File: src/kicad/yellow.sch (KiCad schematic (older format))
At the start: 3 parts, among them U10 74HC08, U8 74HC08, U9 74HC08

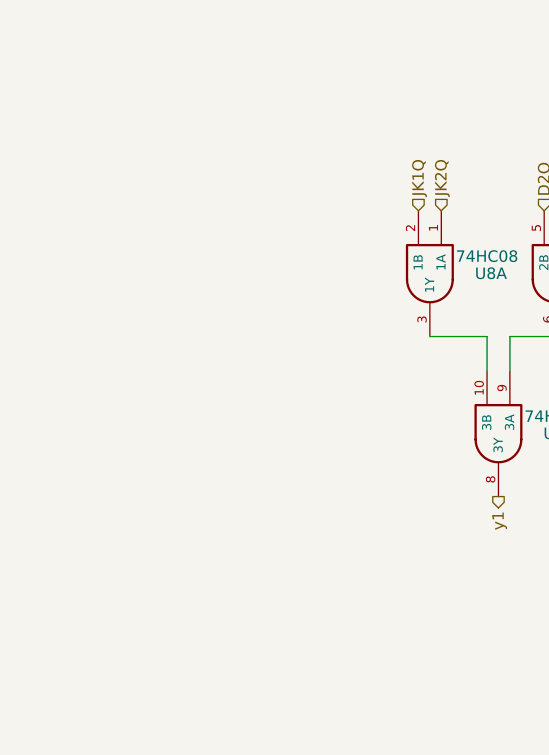
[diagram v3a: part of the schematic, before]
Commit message: added annotations, power connections to parts
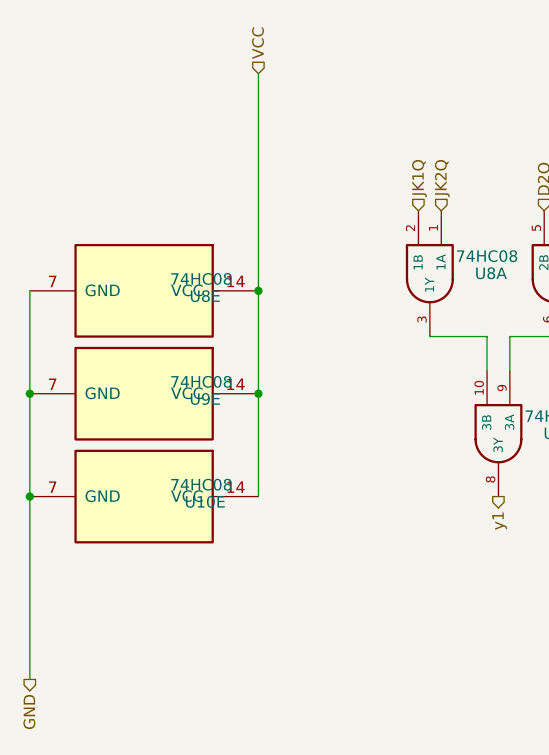
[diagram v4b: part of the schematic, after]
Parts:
- added unit 5 of U10
- added unit 5 of U8
- added unit 5 of U9
- U10, U8, U9: footprint Housings_SOIC:SOIC-14_3.9x8.7mm_Pitch1.27mm -> Package_SO:SOIC-14_3.9x8.7mm_P1.27mm
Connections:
- new net GND: U10.7 (GND), U8.7 (GND), U9.7 (GND)
- new net VCC: U10.14 (VCC), U8.14 (VCC), U9.14 (VCC)
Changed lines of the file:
@@
 F 0 "U8" V 2475 3117 50  0000 C CNN
 F 1 "74HC08" V 2400 3100 50  0000 C CNN
-F 2 "Housings_SOIC:SOIC-14_3.9x8.7mm_Pitch1.27mm" H 2450 2850 50  0001 C CNN
+F 2 "Package_SO:SOIC-14_3.9x8.7mm_P1.27mm" H 2450 2850 50  0001 C CNN
 F 3 "https://datasheet.lcsc.com/szlcsc/Nexperia-74HC08D-653_C5593.pdf" H 2450 2850 50  0001 C CNN
 F 4 "C5593" H 2450 2850 50  0001 C CNN "LCSC"
@@
 F 0 "U8" V 3025 3117 50  0000 C CNN
 F 1 "74HC08" V 2950 3100 50  0000 C CNN
-F 2 "Housings_SOIC:SOIC-14_3.9x8.7mm_Pitch1.27mm" H 3000 2850 50  0001 C CNN
+F 2 "Package_SO:SOIC-14_3.9x8.7mm_P1.27mm" H 3000 2850 50  0001 C CNN
 F 3 "https://datasheet.lcsc.com/szlcsc/Nexperia-74HC08D-653_C5593.pdf" H 3000 2850 50  0001 C CNN
 F 4 "C5593" H 3000 2850 50  0001 C CNN "LCSC"
@@
 F 0 "U8" V 2775 3817 50  0000 C CNN
 F 1 "74HC08" V 2700 3800 50  0000 C CNN
-F 2 "Housings_SOIC:SOIC-14_3.9x8.7mm_Pitch1.27mm" H 2750 3550 50  0001 C CNN
+F 2 "Package_SO:SOIC-14_3.9x8.7mm_P1.27mm" H 2750 3550 50  0001 C CNN
 F 3 "https://datasheet.lcsc.com/szlcsc/Nexperia-74HC08D-653_C5593.pdf" H 2750 3550 50  0001 C CNN
 F 4 "C5593" H 2750 3550 50  0001 C CNN "LCSC"
@@
 F 0 "U8" V 3825 3167 50  0000 C CNN
 F 1 "74HC08" V 3750 3150 50  0000 C CNN
-F 2 "Housings_SOIC:SOIC-14_3.9x8.7mm_Pitch1.27mm" H 3800 2900 50  0001 C CNN
+F 2 "Package_SO:SOIC-14_3.9x8.7mm_P1.27mm" H 3800 2900 50  0001 C CNN
 F 3 "https://datasheet.lcsc.com/szlcsc/Nexperia-74HC08D-653_C5593.pdf" H 3800 2900 50  0001 C CNN
 F 4 "C5593" H 3800 2900 50  0001 C CNN "LCSC"
@@
 F 0 "U9" V 4475 3217 50  0000 C CNN
 F 1 "74HC08" V 4400 3200 50  0000 C CNN
-F 2 "Housings_SOIC:SOIC-14_3.9x8.7mm_Pitch1.27mm" H 4450 2950 50  0001 C CNN
+F 2 "Package_SO:SOIC-14_3.9x8.7mm_P1.27mm" H 4450 2950 50  0001 C CNN
 F 3 "https://datasheet.lcsc.com/szlcsc/Nexperia-74HC08D-653_C5593.pdf" H 4450 2950 50  0001 C CNN
 F 4 "C5593" H 4450 2950 50  0001 C CNN "LCSC"
@@
 F 0 "U9" V 4075 3817 50  0000 C CNN
 F 1 "74HC08" V 4000 3800 50  0000 C CNN
-F 2 "Housings_SOIC:SOIC-14_3.9x8.7mm_Pitch1.27mm" H 4050 3550 50  0001 C CNN
+F 2 "Package_SO:SOIC-14_3.9x8.7mm_P1.27mm" H 4050 3550 50  0001 C CNN
 F 3 "https://datasheet.lcsc.com/szlcsc/Nexperia-74HC08D-653_C5593.pdf" H 4050 3550 50  0001 C CNN
 F 4 "C5593" H 4050 3550 50  0001 C CNN "LCSC"
@@
 F 0 "U9" V 5275 3167 50  0000 C CNN
 F 1 "74HC08" V 5200 3150 50  0000 C CNN
-F 2 "Housings_SOIC:SOIC-14_3.9x8.7mm_Pitch1.27mm" H 5250 2900 50  0001 C CNN
+F 2 "Package_SO:SOIC-14_3.9x8.7mm_P1.27mm" H 5250 2900 50  0001 C CNN
 F 3 "https://datasheet.lcsc.com/szlcsc/Nexperia-74HC08D-653_C5593.pdf" H 5250 2900 50  0001 C CNN
 F 4 "C5593" H 5250 2900 50  0001 C CNN "LCSC"
@@
 F 0 "U9" V 5875 3217 50  0000 C CNN
 F 1 "74HC08" V 5800 3200 50  0000 C CNN
-F 2 "Housings_SOIC:SOIC-14_3.9x8.7mm_Pitch1.27mm" H 5850 2950 50  0001 C CNN
+F 2 "Package_SO:SOIC-14_3.9x8.7mm_P1.27mm" H 5850 2950 50  0001 C CNN
 F 3 "https://datasheet.lcsc.com/szlcsc/Nexperia-74HC08D-653_C5593.pdf" H 5850 2950 50  0001 C CNN
 F 4 "C5593" H 5850 2950 50  0001 C CNN "LCSC"
@@
 F 0 "U10" V 5575 3917 50  0000 C CNN
 F 1 "74HC08" V 5500 3900 50  0000 C CNN
-F 2 "Housings_SOIC:SOIC-14_3.9x8.7mm_Pitch1.27mm" H 5550 3650 50  0001 C CNN
+F 2 "Package_SO:SOIC-14_3.9x8.7mm_P1.27mm" H 5550 3650 50  0001 C CNN
 F 3 "https://datasheet.lcsc.com/szlcsc/Nexperia-74HC08D-653_C5593.pdf" H 5550 3650 50  0001 C CNN
 F 4 "C5593" H 5550 3650 50  0001 C CNN "LCSC"
@@
 F 0 "U10" V 6450 3200 50  0000 C CNN
 F 1 "74HC08" V 6350 3200 50  0000 C CNN
-F 2 "Housings_SOIC:SOIC-14_3.9x8.7mm_Pitch1.27mm" H 6400 2950 50  0001 C CNN
+F 2 "Package_SO:SOIC-14_3.9x8.7mm_P1.27mm" H 6400 2950 50  0001 C CNN
 F 3 "https://datasheet.lcsc.com/szlcsc/Nexperia-74HC08D-653_C5593.pdf" H 6400 2950 50  0001 C CNN
 F 4 "C5593" H 6400 2950 50  0001 C CNN "LCSC"
@@
 F 0 "U10" V 6975 3217 50  0000 C CNN
 F 1 "74HC08" V 6900 3200 50  0000 C CNN
-F 2 "Housings_SOIC:SOIC-14_3.9x8.7mm_Pitch1.27mm" H 6950 2950 50  0001 C CNN
+F 2 "Package_SO:SOIC-14_3.9x8.7mm_P1.27mm" H 6950 2950 50  0001 C CNN
 F 3 "https://datasheet.lcsc.com/szlcsc/Nexperia-74HC08D-653_C5593.pdf" H 6950 2950 50  0001 C CNN
 F 4 "C5593" H 6950 2950 50  0001 C CNN "LCSC"
@@
 F 0 "U10" V 6675 3967 50  0000 C CNN
 F 1 "74HC08" V 6600 3950 50  0000 C CNN
-F 2 "Housings_SOIC:SOIC-14_3.9x8.7mm_Pitch1.27mm" H 6650 3700 50  0001 C CNN
+F 2 "Package_SO:SOIC-14_3.9x8.7mm_P1.27mm" H 6650 3700 50  0001 C CNN
 F 3 "https://datasheet.lcsc.com/szlcsc/Nexperia-74HC08D-653_C5593.pdf" H 6650 3700 50  0001 C CNN
 F 4 "C5593" H 6650 3700 50  0001 C CNN "LCSC"
@@
 Text HLabel 7000 2700 1    50   Input ~ 0
 D2!Q
+$Comp
+L PB170:74HC08 U?
+U 5 1 6060BB07
+P 1200 2950
+AR Path="/6060BB07" Ref="U?"  Part="2"
+AR Path="/6006FC3B/6060BB07" Ref="U?"  Part="4"
+AR Path="/6004480C/6060BB07" Ref="U?"  Part="4"
+AR Path="/60019DBB/6060BB07" Ref="U8"  Part="5"
+F 0 "U8" V 1225 3217 50  0000 C CNN
+F 1 "74HC08" V 1150 3200 50  0000 C CNN
+F 2 "Package_SO:SOIC-14_3.9x8.7mm_P1.27mm" H 1200 2950 50  0001 C CNN
+F 3 "https://datasheet.lcsc.com/szlcsc/Nexperia-74HC08D-653_C5593.pdf" H 1200 2950 50  0001 C CNN
+F 4 "C5593" H 1200 2950 50  0001 C CNN "LCSC"
+	5    1200 2950
+	0    1    1    0
+$EndComp
+$Comp
+L PB170:74HC08 U?
+U 5 1 6060D9E8
+P 1200 3400
+AR Path="/6060D9E8" Ref="U?"  Part="2"
+AR Path="/6006FC3B/6060D9E8" Ref="U?"  Part="4"
+AR Path="/6004480C/6060D9E8" Ref="U?"  Part="4"
+AR Path="/60019DBB/6060D9E8" Ref="U9"  Part="5"
+F 0 "U9" V 1225 3667 50  0000 C CNN
+F 1 "74HC08" V 1150 3650 50  0000 C CNN
+F 2 "Package_SO:SOIC-14_3.9x8.7mm_P1.27mm" H 1200 3400 50  0001 C CNN
+F 3 "https://datasheet.lcsc.com/szlcsc/Nexperia-74HC08D-653_C5593.pdf" H 1200 3400 50  0001 C CNN
+F 4 "C5593" H 1200 3400 50  0001 C CNN "LCSC"
+	5    1200 3400
+	0    1    1    0
+$EndComp
+$Comp
+L PB170:74HC08 U?
+U 5 1 6060E9B8
+P 1200 3850
+AR Path="/6060E9B8" Ref="U?"  Part="2"
+AR Path="/6006FC3B/6060E9B8" Ref="U?"  Part="4"
+AR Path="/6004480C/6060E9B8" Ref="U?"  Part="4"
+AR Path="/60019DBB/6060E9B8" Ref="U10"  Part="5"
+F 0 "U10" V 1225 4117 50  0000 C CNN
+F 1 "74HC08" V 1150 4100 50  0000 C CNN
+F 2 "Package_SO:SOIC-14_3.9x8.7mm_P1.27mm" H 1200 3850 50  0001 C CNN
+F 3 "https://datasheet.lcsc.com/szlcsc/Nexperia-74HC08D-653_C5593.pdf" H 1200 3850 50  0001 C CNN
+F 4 "C5593" H 1200 3850 50  0001 C CNN "LCSC"
+	5    1200 3850
+	0    1    1    0
+$EndComp
+Wire Wire Line
+	700  3400 700  3850
+Connection ~ 700  3850
+Wire Wire Line
+	700  3850 700  4650
+Wire Wire Line
+	700  3400 700  2950
+Connection ~ 700  3400
+Wire Wire Line
+	1700 3850 1700 3400
+Wire Wire Line
+	1700 3400 1700 2950
+Connection ~ 1700 3400
+Wire Wire Line
+	1700 2950 1700 2000
+Connection ~ 1700 2950
+Text HLabel 1700 2000 1    50   Input ~ 0
+VCC
+Text HLabel 700  4650 3    50   Output ~ 0
+GND
 $EndSCHEMATC

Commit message: Corrected negations
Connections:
- net D2!Q renamed D2~Q
- net JK1!Q renamed JK1~Q
- net JK2!Q renamed JK2~Q
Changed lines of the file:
@@
 D2Q
 Text HLabel 4400 2700 1    50   Input ~ 0
-D2!Q
+D2~Q
 Text HLabel 2400 2600 1    50   Input ~ 0
 JK1Q
 Text HLabel 3750 2650 1    50   Input ~ 0
-JK1!Q
+JK1~Q
 Text HLabel 2500 2600 1    50   Input ~ 0
 JK2Q
 Text HLabel 5900 2700 1    50   Input ~ 0
-JK2!Q
+JK2~Q
 Text HLabel 2750 3850 3    50   Output ~ 0
 y1
@@
 JK2Q
 Text HLabel 4500 2700 1    50   Input ~ 0
-D2!Q
+D2~Q
 Text HLabel 5200 2650 1    50   Input ~ 0
-JK1!Q
+JK1~Q
 Text HLabel 5300 2650 1    50   Input ~ 0
 D2Q
 Text HLabel 6350 2700 1    50   Input ~ 0
-JK2!Q
+JK2~Q
 Text HLabel 6450 2700 1    50   Input ~ 0
 JK1Q
@@
 D1Q
 Text HLabel 7000 2700 1    50   Input ~ 0
-D2!Q
-$Comp
-L PB170:74HC08 U?
+D2~Q
+$Comp
+L PB170:74HC08 U?
